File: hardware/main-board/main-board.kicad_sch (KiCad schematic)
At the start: 84 parts, among them J1 USB_C_Receptacle_USB2.0, J2 DNI, J3 Display Connector, J4 Conn_01x02, SW1 SW_Push, SW2 SW_Push, SW3 SW_Push, SW4 SW_Push, SW5 SW_Detect, SW6 SW_Boot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

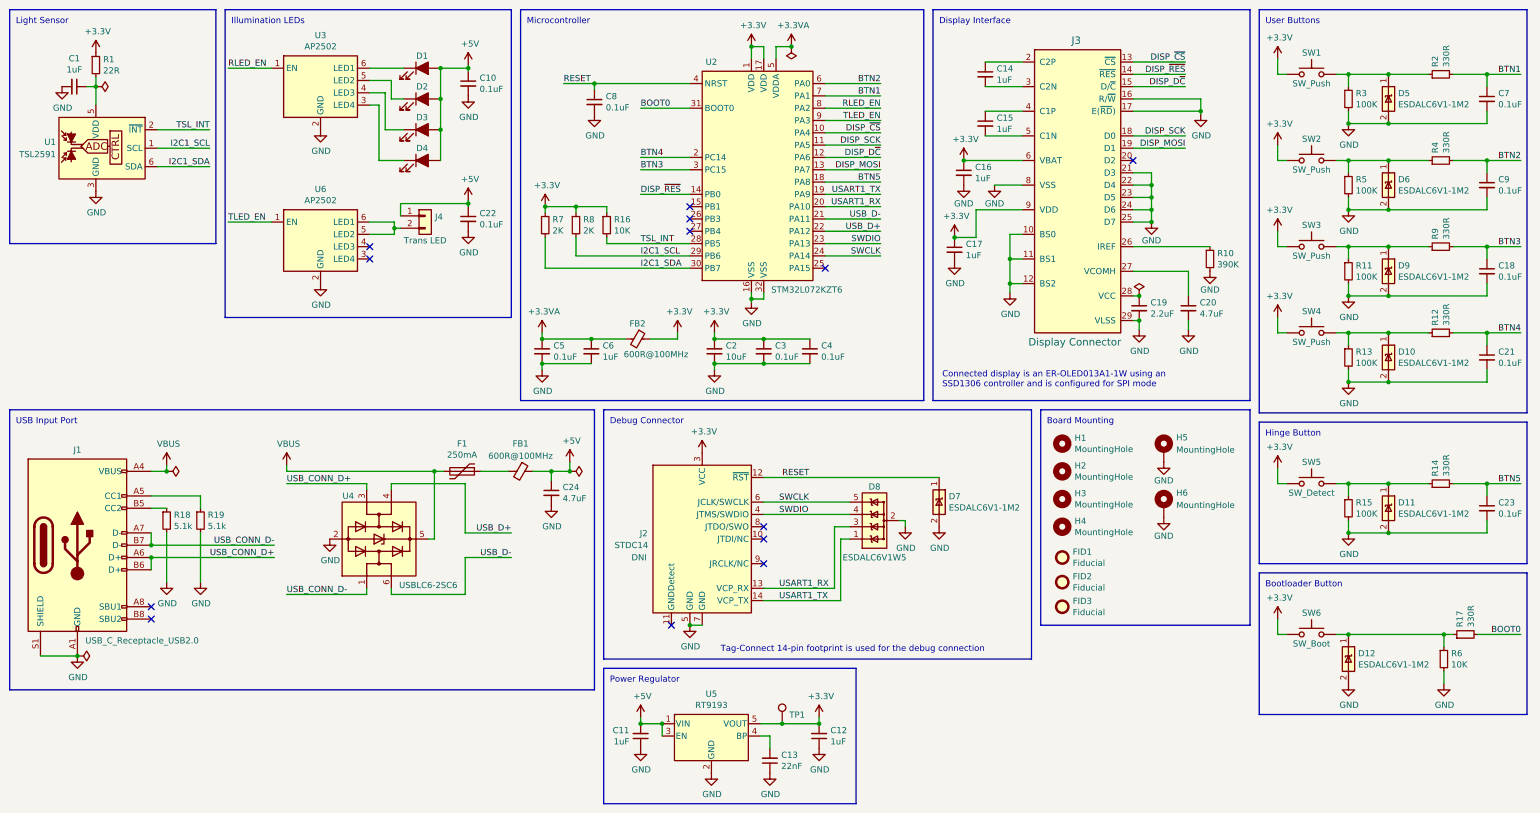
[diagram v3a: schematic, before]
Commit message: Changed LED_EN pins and added pull-down resistors
Switched TLED_EN and RLED_EN pins, per the preceding CubeMX spec update
Added pull-down resistors to TLED_EN, RLED_EN, and DISP_RES to ensure
clean transitions and reliable non-floating behavior during startup and
cases when the firmware hasn't configured these pins yet.

Fix #25
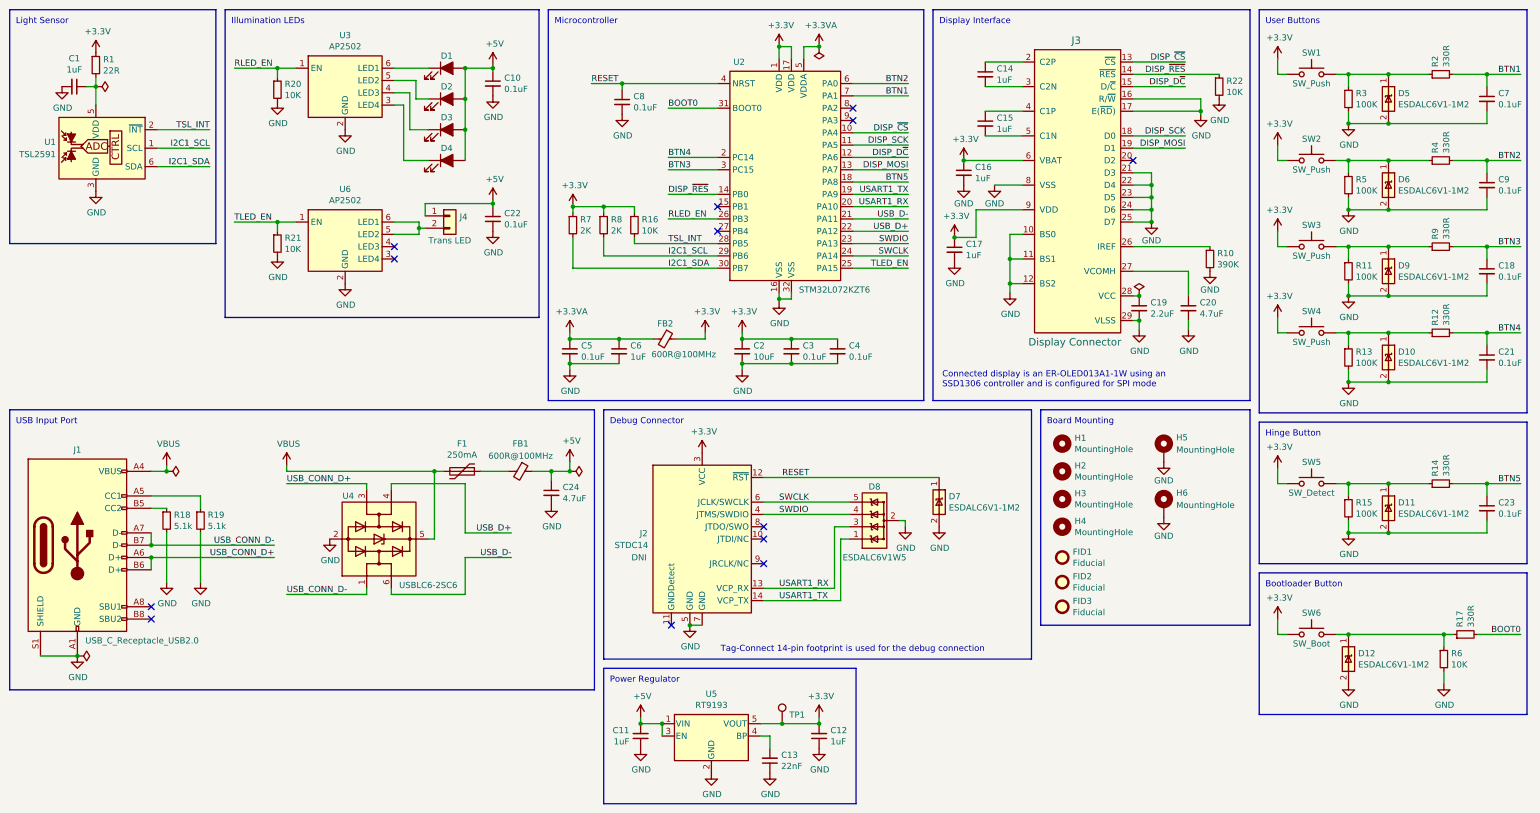
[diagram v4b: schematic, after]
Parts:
- added R20, R21, R22: 10K, Resistor_SMD:R_0603_1608Metric, symbol Device:R_Small
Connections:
- net DISP_~{RES}: now also R22.1
- net GND: now also R20.2, R21.2, R22.2
- net RLED_EN: now also U2.26 (PB3), R20.1; no longer U2.8 (PA2)
- net TLED_EN: now also U2.25 (PA15), R21.1; no longer U2.9 (PA3)
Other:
- moved on the sheet: C10, C2, C22, C3, C4, C5, C6, C8, D1, D2, D3, D4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
